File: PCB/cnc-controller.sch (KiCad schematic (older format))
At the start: 63 parts, among them J1 USB_C_Receptacle, J2 Conn_ARM_JTAG_SWD_10, J3 Conn_01x04, J4 Conn_01x03, Q1 IRLML6402, SW1 SK-12D11VG3, SW10 sw_unit, SW11 sw_unit, SW12 sw_unit, SW13 sw_unit, SW14 sw_unit, SW15 sw_unit, SW16 sw_unit, SW17 sw_unit, SW18 sw_unit, SW19 sw_unit, SW2 SW_Push, SW20 sw_unit, SW21 sw_unit, SW22 sw_unit, SW23 sw_unit, SW24 sw_unit, SW25 sw_unit, SW26 sw_unit, SW3 sw_unit, SW4 sw_unit, SW5 sw_unit, SW6 sw_unit, SW7 sw_unit, SW8 sw_unit, SW9 sw_unit, U1 NJM2884U1-33, U2 SN65220, U3 STM32F042K6Tx

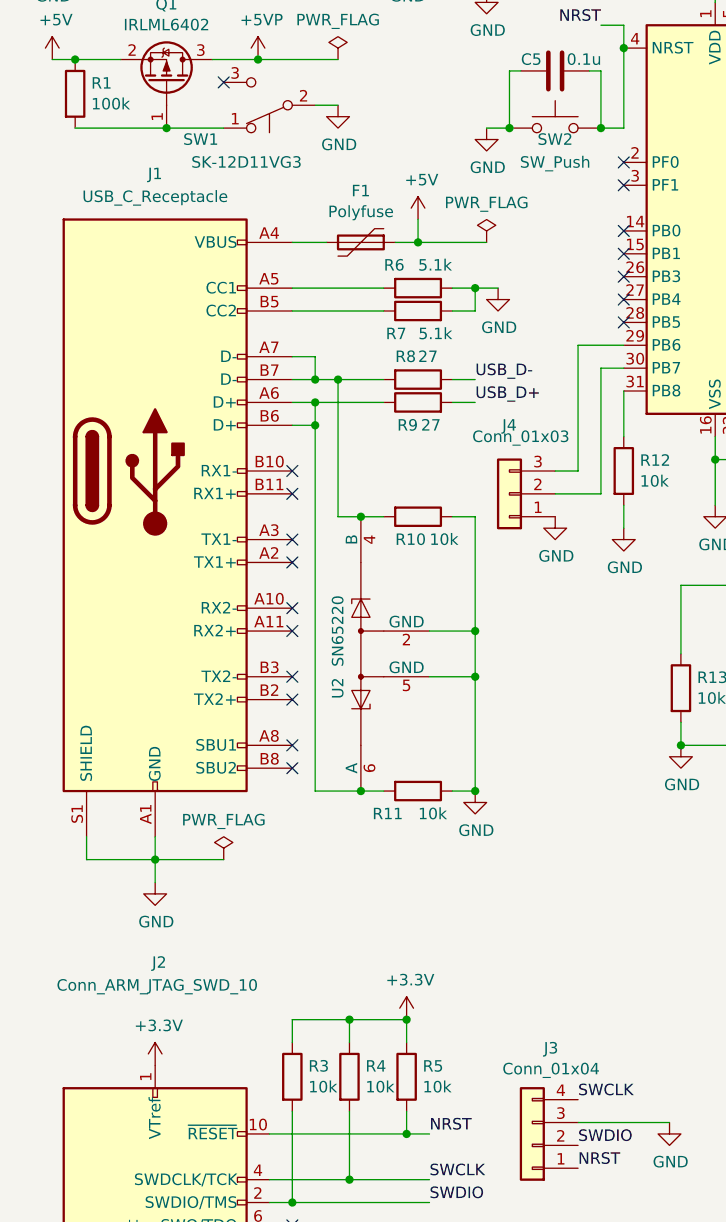
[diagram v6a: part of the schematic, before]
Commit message: 回路図上USBコネクタを2.0用のものに変更
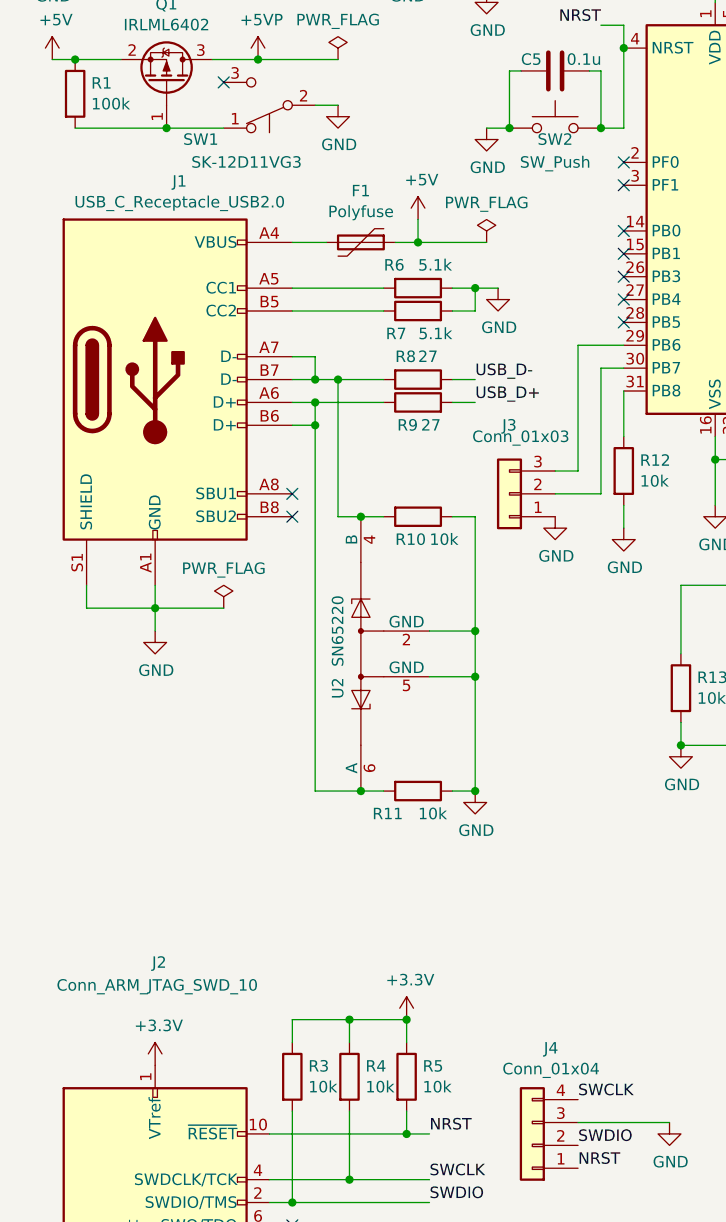
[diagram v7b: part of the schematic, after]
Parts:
- removed J1: USB_C_Receptacle, cnc-controller_Library:USBC_5077CR-16-SMC2-BK-TR, symbol Connector:USB_C_Receptacle
- added J1: USB_C_Receptacle_USB2.0, cnc-controller_Library:USBC_5077CR-16-SMC2-BK-TR, symbol Connector:USB_C_Receptacle_USB2.0
- renumbered J4 to J3, J3 to J4
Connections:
- net GND: now also J1.A1 (GND), J1.A12 (GND), J1.B1 (GND), J1.B12 (GND), J1.S1 (SHIELD)
- net at F1.2: now also J1.A4 (VBUS), J1.A9 (VBUS), J1.B4 (VBUS), J1.B9 (VBUS)
- net at R6.2: now also J1.A5 (CC1)
- net at R11.2, R9.1, U2.6 (A): now also J1.A6 (D+), J1.B6 (D+)
- net at R10.2, R8.2, U2.4 (B): now also J1.A7 (D-), J1.B7 (D-)
- net at R7.1: now also J1.B5 (CC2)
- no-connect marks 22 -> 14
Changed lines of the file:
@@
 	2100 2500 2200 2500
 Wire Wire Line
-	1050 5300 1050 5200
-Connection ~ 1050 5200
+	1050 4200 1050 4100
+Connection ~ 1050 4100
 $Comp
 L power:GND #PWR04
 U 1 1 6111FA4C
-P 1050 5300
-F 0 "#PWR04" H 1050 5050 50  0001 C CNN
-F 1 "GND" H 1055 5127 50  0000 C CNN
-F 2 "" H 1050 5300 50  0001 C CNN
-F 3 "" H 1050 5300 50  0001 C CNN
-	1    1050 5300
-	1    0    0    -1
-$EndComp
-Wire Wire Line
-	1050 5200 1050 5100
-Wire Wire Line
-	750  5200 1050 5200
-Wire Wire Line
-	750  5100 750  5200
-NoConn ~ 1650 4800
-NoConn ~ 1650 4700
-NoConn ~ 1650 4500
-NoConn ~ 1650 4400
-NoConn ~ 1650 4200
-NoConn ~ 1650 4100
-NoConn ~ 1650 3900
-NoConn ~ 1650 3800
-NoConn ~ 1650 3600
-NoConn ~ 1650 3500
+P 1050 4200
+F 0 "#PWR04" H 1050 3950 50  0001 C CNN
+F 1 "GND" H 1055 4027 50  0000 C CNN
+F 2 "" H 1050 4200 50  0001 C CNN
+F 3 "" H 1050 4200 50  0001 C CNN
+	1    1050 4200
+	1    0    0    -1
+$EndComp
+Wire Wire Line
+	1050 4100 1050 4000
+Wire Wire Line
+	750  4100 1050 4100
+Wire Wire Line
+	750  4000 750  4100
 Wire Wire Line
 	1800 2500 1650 2500
@@
 	1    1950 2500
 	0    1    1    0
-$EndComp
-$Comp
-L Connector:USB_C_Receptacle J1
-U 1 1 61101E05
-P 1050 3500
-F 0 "J1" H 1050 4800 50  0000 C CNN
-F 1 "USB_C_Receptacle" H 1050 4700 50  0000 C CNN
-F 2 "cnc-controller_Library:USBC_5077CR-16-SMC2-BK-TR" H 1200 3500 50  0001 C CNN
-F 3 "https://www.usb.org/sites/default/files/documents/usb_type-c.zip" H 1200 3500 50  0001 C CNN
-	1    1050 3500
-	1    0    0    -1
 $EndComp
 $Comp
@@
 	900  1150 900  1250
 $Comp
-L power:PWR_FLAG #FLG01
+L power:PWR_FLAG #FLG03
 U 1 1 613FBC64
 P 2500 2500
-F 0 "#FLG01" H 2500 2575 50  0001 C CNN
+F 0 "#FLG03" H 2500 2575 50  0001 C CNN
 F 1 "PWR_FLAG" H 2500 2673 50  0000 C CNN
 F 2 "" H 2500 2500 50  0001 C CNN
@@
 	7100 6350 7100 6100
 $Comp
-L Connector_Generic:Conn_01x04 J3
+L Connector_Generic:Conn_01x04 J4
 U 1 1 613191D3
 P 2700 6450
-F 0 "J3" H 2618 6025 50  0000 C CNN
+F 0 "J4" H 2618 6025 50  0000 C CNN
 F 1 "Conn_01x04" H 2618 6116 50  0000 C CNN
 F 2 "Connector_PinHeader_2.54mm:PinHeader_1x04_P2.54mm_Vertical" H 2700 6450 50  0001 C CNN
@@
 	2800 3600 3000 3600
 $Comp
-L Connector_Generic:Conn_01x03 J4
+L Connector_Generic:Conn_01x03 J3
 U 1 1 614A6076
 P 2600 3600
-F 0 "J4" H 2600 3300 50  0000 C CNN
+F 0 "J3" H 2600 3300 50  0000 C CNN
 F 1 "Conn_01x03" H 2550 3350 50  0000 C CNN
 F 2 "Connector_PinHeader_2.54mm:PinHeader_1x03_P2.54mm_Vertical" H 2600 3600 50  0001 C CNN
@@
 $EndComp
 $Comp
-L power:PWR_FLAG #FLG0101
+L power:PWR_FLAG #FLG01
 U 1 1 615FE0D6
-P 1350 5200
-F 0 "#FLG0101" H 1350 5275 50  0001 C CNN
-F 1 "PWR_FLAG" H 1350 5373 50  0000 C CNN
-F 2 "" H 1350 5200 50  0001 C CNN
-F 3 "~" H 1350 5200 50  0001 C CNN
-	1    1350 5200
-	1    0    0    -1
-$EndComp
-Wire Wire Line
-	1050 5200 1350 5200
-$Comp
-L power:PWR_FLAG #FLG0102
+P 1350 4100
+F 0 "#FLG01" H 1350 4175 50  0001 C CNN
+F 1 "PWR_FLAG" H 1350 4273 50  0000 C CNN
+F 2 "" H 1350 4100 50  0001 C CNN
+F 3 "~" H 1350 4100 50  0001 C CNN
+	1    1350 4100
+	1    0    0    -1
+$EndComp
+Wire Wire Line
+	1050 4100 1350 4100
+$Comp
+L power:PWR_FLAG #FLG02
 U 1 1 61625C93
 P 1850 1700
-F 0 "#FLG0102" H 1850 1775 50  0001 C CNN
+F 0 "#FLG02" H 1850 1775 50  0001 C CNN
 F 1 "PWR_FLAG" H 1850 1873 50  0000 C CNN
 F 2 "" H 1850 1700 50  0001 C CNN
@@
 	1500 1700 1850 1700
 Connection ~ 1500 1700
+$Comp
+L Connector:USB_C_Receptacle_USB2.0 J1
+U 1 1 611DFB0E
+P 1050 3100
+F 0 "J1" H 1157 3967 50  0000 C CNN
+F 1 "USB_C_Receptacle_USB2.0" H 1157 3876 50  0000 C CNN
+F 2 "cnc-controller_Library:USBC_5077CR-16-SMC2-BK-TR" H 1200 3100 50  0001 C CNN
+F 3 "https://www.usb.org/sites/default/files/documents/usb_type-c.zip" H 1200 3100 50  0001 C CNN
+	1    1050 3100
+	1    0    0    -1
+$EndComp
+NoConn ~ 1650 3600
+NoConn ~ 1650 3700
 $EndSCHEMATC

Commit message: 基板の作成を開始 あらかた終了したが、外形線との間隔をあける必要あり
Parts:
- R10, R11: value 10k -> 15k
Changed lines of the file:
@@
 P 2200 3700
 F 0 "R10" V 2300 3600 50  0000 L CNN
-F 1 "10k" V 2300 3750 50  0000 L CNN
+F 1 "15k" V 2300 3750 50  0000 L CNN
 F 2 "Resistor_SMD:R_0603_1608Metric_Pad0.98x0.95mm_HandSolder" V 2130 3700 50  0001 C CNN
 F 3 "~" H 2200 3700 50  0001 C CNN
@@
 P 2200 4900
 F 0 "R11" V 2300 4700 50  0000 L CNN
-F 1 "10k" V 2300 4900 50  0000 L CNN
+F 1 "15k" V 2300 4900 50  0000 L CNN
 F 2 "Resistor_SMD:R_0603_1608Metric_Pad0.98x0.95mm_HandSolder" V 2130 4900 50  0001 C CNN
 F 3 "~" H 2200 4900 50  0001 C CNN
@@
 	2450 3200 2350 3200
 Connection ~ 2450 4400
-Connection ~ 1950 4900
-Wire Wire Line
-	2050 4900 1950 4900
-Wire Wire Line
-	2050 3700 1950 3700
 Wire Wire Line
 	2450 4400 2450 4200
@@
 Wire Wire Line
 	2350 4900 2450 4900
-Wire Wire Line
-	1750 4900 1950 4900
-Wire Wire Line
-	1850 3700 1950 3700
-Connection ~ 1950 3700
 Connection ~ 2450 4900
 Wire Wire Line
@@
 NoConn ~ 1650 3600
 NoConn ~ 1650 3700
+Wire Wire Line
+	1950 3700 2050 3700
+Wire Wire Line
+	1950 3700 1850 3700
+Connection ~ 1950 3700
+Wire Wire Line
+	2050 4900 1950 4900
+Wire Wire Line
+	1950 4900 1750 4900
+Connection ~ 1950 4900
 $EndSCHEMATC
